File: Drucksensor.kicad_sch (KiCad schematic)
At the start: 51 parts, among them J101 Conn_01x02, J102 Start, J103 RJ45, J104 RJ45, J105 DB15_Female_MountingHoles, J106 Serial, Q101 Q_NMOS_GSD, Q102 Q_NMOS_GSD, Q103 Q_NMOS_GSD, SW101 SW_DPST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

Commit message: Lüfter Eingefügt
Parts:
- added J107: Conn_01x03_Male, Connector_PinSocket_2.54mm:PinSocket_1x03_P2.54mm_Vertical, symbol Connector:Conn_01x03_Male
- added R121: 10, Resistor_SMD:R_0603_1608Metric, symbol Device:R
- added R122: 10k, Resistor_SMD:R_0603_1608Metric, symbol Device:R
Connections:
- net 24_Ext: now also J107.1 (Pin_1)
- net 7SegClk: now also A101.20 (D5); no longer A101.18 (D3)
- net 7SegData: now also A101.18 (D3); no longer A101.17 (D2)
- net GND: now also J107.3 (Pin_3), R122.1
- net Magnetron_Enable: now also R122.2
- new net: J107.2 (Pin_2), R121.2
- new net Tacho: A101.17 (D2), R121.1
- no-connect marks 21 -> 20
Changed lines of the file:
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@@
   (no_connect (at 165.1 57.15))
   (no_connect (at 165.1 67.31))
-  (no_connect (at 224.79 101.6))
   (no_connect (at 224.79 109.22))
   (no_connect (at 224.79 111.76))
@@
     (stroke (width 0) (type solid) (color 0 0 0 0))
   )
+  (wire (pts (xy 201.93 93.98) (xy 205.74 93.98))
+    (stroke (width 0) (type solid) (color 0 0 0 0))
+  )
+  (wire (pts (xy 213.36 93.98) (xy 224.79 93.98))
+    (stroke (width 0) (type solid) (color 0 0 0 0))
+  )
   (wire (pts (xy 220.98 26.67) (xy 220.98 39.37))
     (stroke (width 0) (type solid) (color 0 0 0 0))
@@
     (effects (font (size 1.27 1.27)) (justify left bottom))
   )
+  (label "Magnetron_Enable" (at 165.1 149.86 90)
+    (effects (font (size 1.27 1.27)) (justify left bottom))
+  )
   (label "TX" (at 196.85 52.07 0)
     (effects (font (size 1.27 1.27)) (justify left bottom))
@@
     (effects (font (size 1.27 1.27)) (justify left bottom))
   )
+  (label "24_Ext" (at 201.93 91.44 0)
+    (effects (font (size 1.27 1.27)) (justify left bottom))
+  )
+  (label "Tacho" (at 219.71 93.98 180)
+    (effects (font (size 1.27 1.27)) (justify right bottom))
+  )
   (label "TX" (at 224.79 88.9 180)
     (effects (font (size 1.27 1.27)) (justify right bottom))
@@
     (effects (font (size 1.27 1.27)) (justify right bottom))
   )
-  (label "7SegData" (at 224.79 93.98 180)
-    (effects (font (size 1.27 1.27)) (justify right bottom))
-  )
-  (label "7SegClk" (at 224.79 96.52 180)
+  (label "7SegData" (at 224.79 96.52 180)
     (effects (font (size 1.27 1.27)) (justify right bottom))
   )
   (label "7SegEN" (at 224.79 99.06 180)
+    (effects (font (size 1.27 1.27)) (justify right bottom))
+  )
+  (label "7SegClk" (at 224.79 101.6 180)
     (effects (font (size 1.27 1.27)) (justify right bottom))
   )
@@
     (pin "1")
   )
+  (symbol (lib_id "power:GND") (at 165.1 157.48 0) (unit 1)
+    (in_bom yes) (on_board yes) (fields_autoplaced)
+    (property "Reference" "#PWR0158" (id 0) (at 165.1 163.83 0)
+      (effects (font (size 1.27 1.27)) hide)
+    )
+    (property "Value" "GND" (id 1) (at 165.1 161.8044 0))
+    (property "Footprint" "" (id 2) (at 165.1 157.48 0)
+      (effects (font (size 1.27 1.27)) hide)
+    )
+    (property "Datasheet" "" (id 3) (at 165.1 157.48 0)
+      (effects (font (size 1.27 1.27)) hide)
+    )
+    (pin "1")
+  )
   (symbol (lib_id "power:GND") (at 172.72 39.37 90) (unit 1)
     (in_bom yes) (on_board yes) (fields_autoplaced)
@@
     )
     (property "Datasheet" "" (id 3) (at 181.61 33.02 0)
+      (effects (font (size 1.27 1.27)) hide)
+    )
+    (pin "1")
+  )
+  (symbol (lib_id "power:GND") (at 201.93 96.52 0) (unit 1)
+    (in_bom yes) (on_board yes) (fields_autoplaced)
+    (property "Reference" "#PWR0157" (id 0) (at 201.93 102.87 0)
+      (effects (font (size 1.27 1.27)) hide)
+    )
+    (property "Value" "GND" (id 1) (at 201.93 100.8444 0))
+    (property "Footprint" "" (id 2) (at 201.93 96.52 0)
+      (effects (font (size 1.27 1.27)) hide)
+    )
+    (property "Datasheet" "" (id 3) (at 201.93 96.52 0)
       (effects (font (size 1.27 1.27)) hide)
     )
@@
     (pin "2")
   )
+  (symbol (lib_id "Device:R") (at 165.1 153.67 180) (unit 1)
+    (in_bom yes) (on_board yes) (fields_autoplaced)
+    (property "Reference" "R122" (id 0) (at 166.8781 152.9091 0)
+      (effects (font (size 1.27 1.27)) (justify right))
+    )
+    (property "Value" "10k" (id 1) (at 166.8781 155.2078 0)
+      (effects (font (size 1.27 1.27)) (justify right))
+    )
+    (property "Footprint" "Resistor_SMD:R_0603_1608Metric" (id 2) (at 166.878 153.67 90)
+      (effects (font (size 1.27 1.27)) hide)
+    )
+    (property "Datasheet" "~" (id 3) (at 165.1 153.67 0)
+      (effects (font (size 1.27 1.27)) hide)
+    )
+    (pin "1")
+    (pin "2")
+  )
   (symbol (lib_id "Device:R") (at 193.04 52.07 90) (unit 1)
     (in_bom yes) (on_board yes) (fields_autoplaced)
@@
     (pin "2")
   )
+  (symbol (lib_id "Device:R") (at 209.55 93.98 270) (unit 1)
+    (in_bom yes) (on_board yes) (fields_autoplaced)
+    (property "Reference" "R121" (id 0) (at 209.55 89.5308 90))
+    (property "Value" "10" (id 1) (at 209.55 91.8295 90))
+    (property "Footprint" "Resistor_SMD:R_0603_1608Metric" (id 2) (at 209.55 92.202 90)
+      (effects (font (size 1.27 1.27)) hide)
+    )
+    (property "Datasheet" "~" (id 3) (at 209.55 93.98 0)
+      (effects (font (size 1.27 1.27)) hide)
+    )
+    (pin "1")
+    (pin "2")
+  )
   (symbol (lib_id "Device:R") (at 265.43 129.54 0) (unit 1)
     (in_bom yes) (on_board yes) (fields_autoplaced)
@@
     (pin "1")
     (pin "2")
+  )
+  (symbol (lib_id "Connector:Conn_01x03_Male") (at 196.85 93.98 0) (unit 1)
+    (in_bom yes) (on_board yes) (fields_autoplaced)
+    (property "Reference" "J107" (id 0) (at 199.5424 87.7528 0))
+    (property "Value" "Conn_01x03_Male" (id 1) (at 199.5424 90.0515 0))
+    (property "Footprint" "Connector_PinSocket_2.54mm:PinSocket_1x03_P2.54mm_Vertical" (id 2) (at 196.85 93.98 0)
+      (effects (font (size 1.27 1.27)) hide)
+    )
+    (property "Datasheet" "~" (id 3) (at 196.85 93.98 0)
+      (effects (font (size 1.27 1.27)) hide)
+    )
+    (pin "1")
+    (pin "2")
+    (pin "3")
   )
   (symbol (lib_id "Connector_Generic:Conn_01x02") (at 25.4 50.8 0) (mirror y) (unit 1)
@@
       (reference "#PWR0156") (unit 1) (value "GND") (footprint "")
     )
+    (path "/e436bdd1-9cb4-4b56-be2c-8fcebc222123"
+      (reference "#PWR0157") (unit 1) (value "GND") (footprint "")
+    )
+    (path "/3618059e-0e04-4b85-ab17-4ae7ad77943e"
+      (reference "#PWR0158") (unit 1) (value "GND") (footprint "")
+    )
     (path "/e503707e-06bf-4f70-9bbb-eb4903f114d0"
       (reference "#PWR0159") (unit 1) (value "GND") (footprint "")
@@
       (reference "J106") (unit 1) (value "Serial") (footprint "Connector_PinSocket_2.54mm:PinSocket_1x02_P2.54mm_Vertical")
     )
+    (path "/19f52938-4be4-4bc1-a9e1-c911a670bf37"
+      (reference "J107") (unit 1) (value "Conn_01x03_Male") (footprint "Connector_PinSocket_2.54mm:PinSocket_1x03_P2.54mm_Vertical")
+    )
     (path "/13b995c7-480d-4bb7-871d-484d08bb7df3"
       (reference "Q101") (unit 1) (value "Q_NMOS_GSD") (footprint "Package_TO_SOT_SMD:SOT-23")
@@
       (reference "R120") (unit 1) (value "10k") (footprint "Resistor_SMD:R_0603_1608Metric")
     )
+    (path "/2dbdfdf5-62bc-481a-ab86-cf902a70ae15"
+      (reference "R121") (unit 1) (value "10") (footprint "Resistor_SMD:R_0603_1608Metric")
+    )
+    (path "/8ed7b08e-5754-4eec-8fb2-79719519f346"
+      (reference "R122") (unit 1) (value "10k") (footprint "Resistor_SMD:R_0603_1608Metric")
+    )
     (path "/ff0f71b4-ca04-499c-a8af-368cdaf2e1e2"

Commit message: Software-Serial für RS232 interface
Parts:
- added R123, R124: Open, Resistor_SMD:R_0805_2012Metric, symbol Device:R
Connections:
- net RX: now also R123.1; no longer R116.2, U102.12 (R1OUT)
- net TX: now also R124.1; no longer R105.2, U102.11 (T1IN)
- net TX_2: now reaches A101.23 (D8)
- net TX_2: now also R105.2, U102.11 (T1IN), R124.2
- net RX_2: now reaches A101.24 (D9)
- net RX_2: now also R116.2, U102.12 (R1OUT), R123.2
- no-connect marks 20 -> 18
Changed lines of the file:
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@@
   (no_connect (at 165.1 57.15))
   (no_connect (at 165.1 67.31))
-  (no_connect (at 224.79 109.22))
-  (no_connect (at 224.79 111.76))
   (no_connect (at 224.79 116.84))
   (no_connect (at 224.79 121.92))
@@
     (effects (font (size 1.27 1.27)) (justify right bottom))
   )
-  (label "TX" (at 124.46 52.07 180)
-    (effects (font (size 1.27 1.27)) (justify right bottom))
-  )
-  (label "RX" (at 124.46 62.23 180)
+  (label "TX_2" (at 124.46 52.07 180)
+    (effects (font (size 1.27 1.27)) (justify right bottom))
+  )
+  (label "RX_2" (at 124.46 62.23 180)
     (effects (font (size 1.27 1.27)) (justify right bottom))
   )
@@
     (effects (font (size 1.27 1.27)) (justify left bottom))
   )
-  (label "TX" (at 196.85 52.07 0)
+  (label "RX" (at 189.23 71.12 180)
+    (effects (font (size 1.27 1.27)) (justify right bottom))
+  )
+  (label "TX" (at 189.23 77.47 180)
+    (effects (font (size 1.27 1.27)) (justify right bottom))
+  )
+  (label "TX_2" (at 196.85 52.07 0)
     (effects (font (size 1.27 1.27)) (justify left bottom))
   )
-  (label "RX" (at 196.85 62.23 0)
+  (label "RX_2" (at 196.85 62.23 0)
+    (effects (font (size 1.27 1.27)) (justify left bottom))
+  )
+  (label "RX_2" (at 196.85 71.12 0)
+    (effects (font (size 1.27 1.27)) (justify left bottom))
+  )
+  (label "TX_2" (at 196.85 77.47 0)
     (effects (font (size 1.27 1.27)) (justify left bottom))
   )
@@
   )
   (label "Magnetron_Enable" (at 224.79 106.68 180)
+    (effects (font (size 1.27 1.27)) (justify right bottom))
+  )
+  (label "TX_2" (at 224.79 109.22 180)
+    (effects (font (size 1.27 1.27)) (justify right bottom))
+  )
+  (label "RX_2" (at 224.79 111.76 180)
     (effects (font (size 1.27 1.27)) (justify right bottom))
   )
@@
     )
     (property "Datasheet" "~" (id 3) (at 193.04 62.23 0)
+      (effects (font (size 1.27 1.27)) hide)
+    )
+    (pin "1")
+    (pin "2")
+  )
+  (symbol (lib_id "Device:R") (at 193.04 71.12 90) (unit 1)
+    (in_bom yes) (on_board yes) (fields_autoplaced)
+    (property "Reference" "R123" (id 0) (at 193.04 66.6708 90))
+    (property "Value" "Open" (id 1) (at 193.04 68.9695 90))
+    (property "Footprint" "Resistor_SMD:R_0805_2012Metric" (id 2) (at 193.04 72.898 90)
+      (effects (font (size 1.27 1.27)) hide)
+    )
+    (property "Datasheet" "~" (id 3) (at 193.04 71.12 0)
+      (effects (font (size 1.27 1.27)) hide)
+    )
+    (pin "1")
+    (pin "2")
+  )
+  (symbol (lib_id "Device:R") (at 193.04 77.47 90) (unit 1)
+    (in_bom yes) (on_board yes) (fields_autoplaced)
+    (property "Reference" "R124" (id 0) (at 193.04 73.0208 90))
+    (property "Value" "Open" (id 1) (at 193.04 75.3195 90))
+    (property "Footprint" "Resistor_SMD:R_0805_2012Metric" (id 2) (at 193.04 79.248 90)
+      (effects (font (size 1.27 1.27)) hide)
+    )
+    (property "Datasheet" "~" (id 3) (at 193.04 77.47 0)
       (effects (font (size 1.27 1.27)) hide)
     )
@@
       (reference "R122") (unit 1) (value "10k") (footprint "Resistor_SMD:R_0603_1608Metric")
     )
+    (path "/4e259b18-3895-43bb-8edc-75ba343d6625"
+      (reference "R123") (unit 1) (value "Open") (footprint "Resistor_SMD:R_0805_2012Metric")
+    )
+    (path "/a3fe113a-b47d-4938-94c6-19c8889276f3"
+      (reference "R124") (unit 1) (value "Open") (footprint "Resistor_SMD:R_0805_2012Metric")
+    )
     (path "/ff0f71b4-ca04-499c-a8af-368cdaf2e1e2"

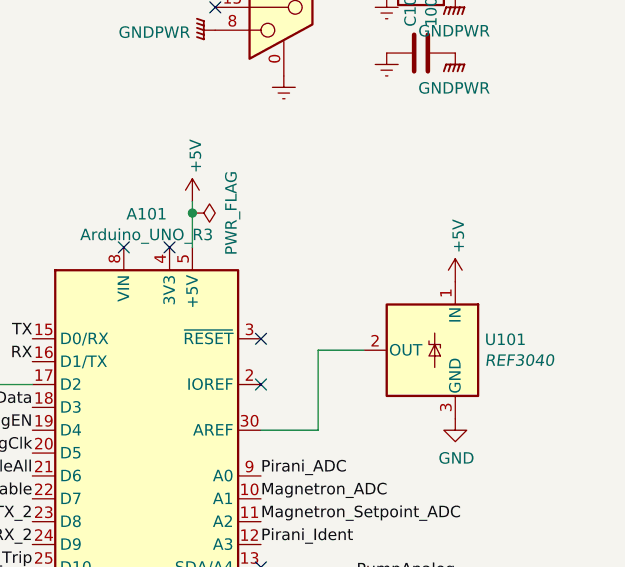
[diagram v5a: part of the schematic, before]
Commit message: Kondensatoren für V-Ref
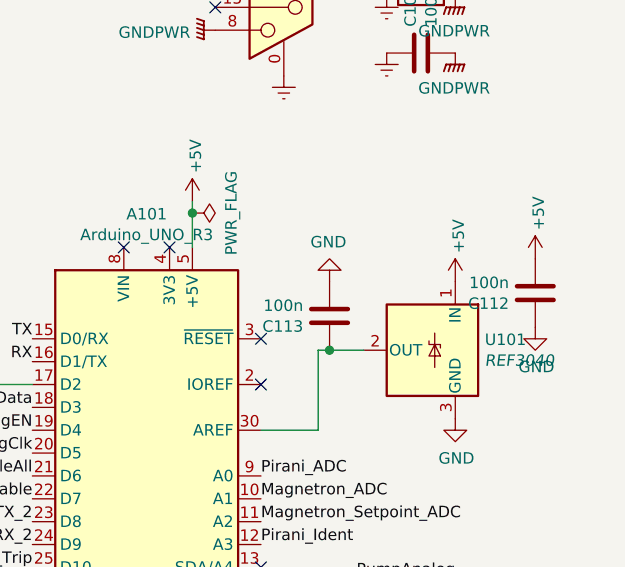
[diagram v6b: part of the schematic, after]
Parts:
- added C112, C113: 100n, Capacitor_SMD:C_0603_1608Metric, symbol Device:C
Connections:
- net +5V: now also C112.2
- net GND: now also C112.1, C113.2
- net at A101.30 (AREF), U101.2 (OUT): now also C113.1
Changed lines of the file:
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@@
   (junction (at 223.52 26.67) (diameter 1.016) (color 0 0 0 0))
   (junction (at 242.57 74.93) (diameter 1.016) (color 0 0 0 0))
+  (junction (at 257.81 90.17) (diameter 1.016) (color 0 0 0 0))
   (junction (at 265.43 124.46) (diameter 1.016) (color 0 0 0 0))
   (junction (at 269.24 124.46) (diameter 1.016) (color 0 0 0 0))
@@
     (stroke (width 0) (type solid) (color 0 0 0 0))
   )
-  (wire (pts (xy 261.62 90.17) (xy 256.54 90.17))
+  (wire (pts (xy 257.81 90.17) (xy 256.54 90.17))
+    (stroke (width 0) (type solid) (color 0 0 0 0))
+  )
+  (wire (pts (xy 261.62 90.17) (xy 257.81 90.17))
     (stroke (width 0) (type solid) (color 0 0 0 0))
   )
@@
     (pin "1")
   )
+  (symbol (lib_id "power:+5V") (at 280.67 80.01 0) (unit 1)
+    (in_bom yes) (on_board yes)
+    (property "Reference" "#PWR0162" (id 0) (at 280.67 83.82 0)
+      (effects (font (size 1.27 1.27)) hide)
+    )
+    (property "Value" "+5V" (id 1) (at 281.0383 76.8349 90)
+      (effects (font (size 1.27 1.27)) (justify left))
+    )
+    (property "Footprint" "" (id 2) (at 280.67 80.01 0)
+      (effects (font (size 1.27 1.27)) hide)
+    )
+    (property "Datasheet" "" (id 3) (at 280.67 80.01 0)
+      (effects (font (size 1.27 1.27)) hide)
+    )
+    (pin "1")
+  )
   (symbol (lib_id "power:PWR_FLAG") (at 31.75 53.34 180) (unit 1)
     (in_bom yes) (on_board yes)
@@
     (pin "1")
   )
+  (symbol (lib_id "power:GND") (at 257.81 82.55 180) (unit 1)
+    (in_bom yes) (on_board yes)
+    (property "Reference" "#PWR0163" (id 0) (at 257.81 76.2 0)
+      (effects (font (size 1.27 1.27)) hide)
+    )
+    (property "Value" "GND" (id 1) (at 257.683 78.1558 0))
+    (property "Footprint" "" (id 2) (at 257.81 82.55 0)
+      (effects (font (size 1.27 1.27)) hide)
+    )
+    (property "Datasheet" "" (id 3) (at 257.81 82.55 0)
+      (effects (font (size 1.27 1.27)) hide)
+    )
+    (pin "1")
+  )
   (symbol (lib_id "power:Earth") (at 264.16 50.8 0) (unit 1)
     (in_bom yes) (on_board yes) (fields_autoplaced)
@@
     )
     (property "Datasheet" "" (id 3) (at 276.86 133.35 0)
+      (effects (font (size 1.27 1.27)) hide)
+    )
+    (pin "1")
+  )
+  (symbol (lib_id "power:GND") (at 280.67 87.63 0) (unit 1)
+    (in_bom yes) (on_board yes)
+    (property "Reference" "#PWR0164" (id 0) (at 280.67 93.98 0)
+      (effects (font (size 1.27 1.27)) hide)
+    )
+    (property "Value" "GND" (id 1) (at 280.797 92.0242 0))
+    (property "Footprint" "" (id 2) (at 280.67 87.63 0)
+      (effects (font (size 1.27 1.27)) hide)
+    )
+    (property "Datasheet" "" (id 3) (at 280.67 87.63 0)
       (effects (font (size 1.27 1.27)) hide)
     )
@@
     (pin "2")
   )
+  (symbol (lib_id "Device:C") (at 257.81 86.36 180) (unit 1)
+    (in_bom yes) (on_board yes)
+    (property "Reference" "C113" (id 0) (at 254.889 87.5284 0)
+      (effects (font (size 1.27 1.27)) (justify left))
+    )
+    (property "Value" "100n" (id 1) (at 254.889 85.217 0)
+      (effects (font (size 1.27 1.27)) (justify left))
+    )
+    (property "Footprint" "Capacitor_SMD:C_0603_1608Metric" (id 2) (at 256.8448 82.55 0)
+      (effects (font (size 1.27 1.27)) hide)
+    )
+    (property "Datasheet" "~" (id 3) (at 257.81 86.36 0)
+      (effects (font (size 1.27 1.27)) hide)
+    )
+    (pin "1")
+    (pin "2")
+  )
   (symbol (lib_id "Device:C") (at 267.97 57.15 90) (unit 1)
     (in_bom yes) (on_board yes)
@@
     )
     (property "Datasheet" "~" (id 3) (at 276.86 129.54 0)
+      (effects (font (size 1.27 1.27)) hide)
+    )
+    (pin "1")
+    (pin "2")
+  )
+  (symbol (lib_id "Device:C") (at 280.67 83.82 180) (unit 1)
+    (in_bom yes) (on_board yes)
+    (property "Reference" "C112" (id 0) (at 277.749 84.9884 0)
+      (effects (font (size 1.27 1.27)) (justify left))
+    )
+    (property "Value" "100n" (id 1) (at 277.749 82.677 0)
+      (effects (font (size 1.27 1.27)) (justify left))
+    )
+    (property "Footprint" "Capacitor_SMD:C_0603_1608Metric" (id 2) (at 279.7048 80.01 0)
+      (effects (font (size 1.27 1.27)) hide)
+    )
+    (property "Datasheet" "~" (id 3) (at 280.67 83.82 0)
       (effects (font (size 1.27 1.27)) hide)
     )
@@
       (reference "#PWR0161") (unit 1) (value "GND") (footprint "")
     )
+    (path "/68d20063-c7d2-41ea-92fa-b8dd3d81a455"
+      (reference "#PWR0162") (unit 1) (value "+5V") (footprint "")
+    )
+    (path "/d77f6bba-3c71-444c-a7f1-2c5d3eb0a097"
+      (reference "#PWR0163") (unit 1) (value "GND") (footprint "")
+    )
+    (path "/d875fa79-d96c-4e21-bf4b-da1357ba1533"
+      (reference "#PWR0164") (unit 1) (value "GND") (footprint "")
+    )
     (path "/88276ede-ec0f-4f9f-9998-4699edeb1bbe"
       (reference "A101") (unit 1) (value "Arduino_UNO_R3") (footprint "Module:Arduino_UNO_R3")
@@
       (reference "C111") (unit 1) (value "100n") (footprint "Capacitor_SMD:C_0603_1608Metric")
     )
+    (path "/488835d0-a8d7-4626-9477-9e6a1a32d526"
+      (reference "C112") (unit 1) (value "100n") (footprint "Capacitor_SMD:C_0603_1608Metric")
+    )
+    (path "/d886d1b8-debd-4fea-8c08-4e481fb68afc"
+      (reference "C113") (unit 1) (value "100n") (footprint "Capacitor_SMD:C_0603_1608Metric")
+    )
     (path "/2872d14a-5ae9-4893-b0e2-593afe363857"
